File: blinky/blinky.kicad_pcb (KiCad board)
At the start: 2 copper layers, 25.4 x 25.4 mm, 7 parts, among them U1 7555

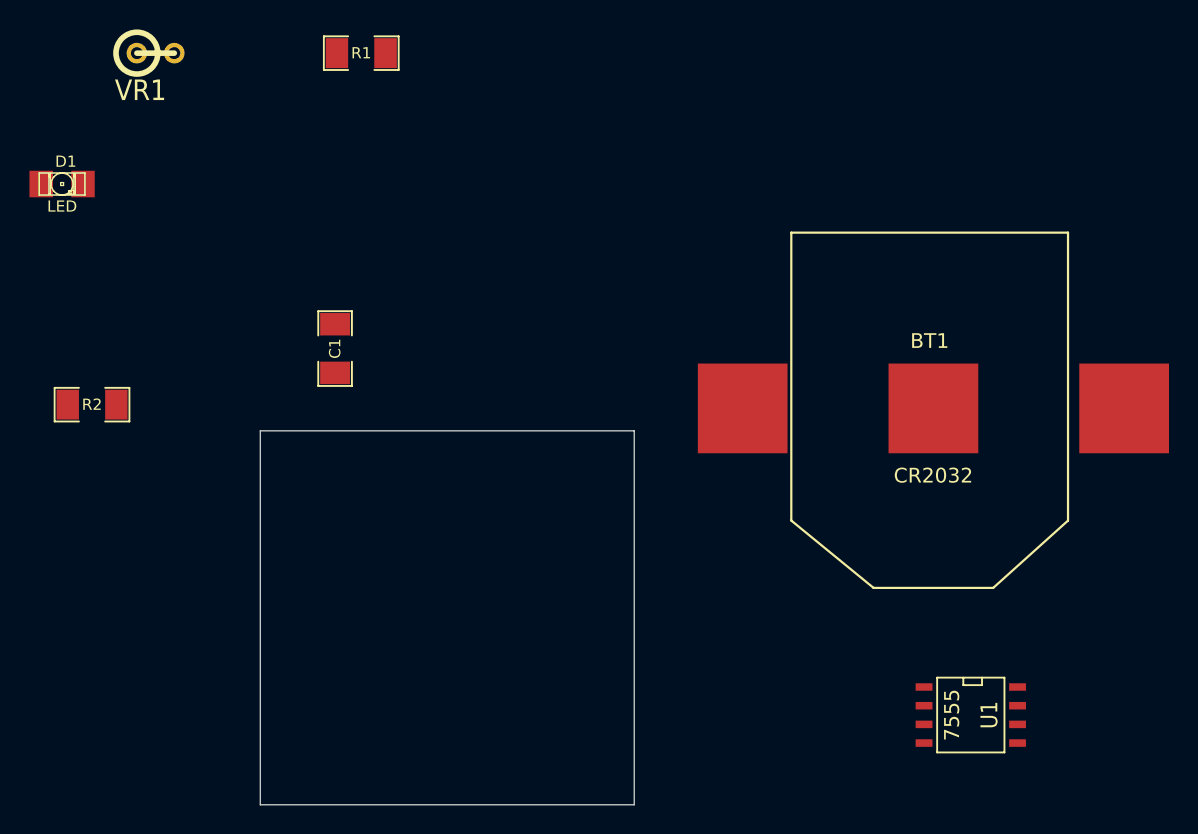
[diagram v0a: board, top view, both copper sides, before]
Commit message: Added gerbers and did layout.
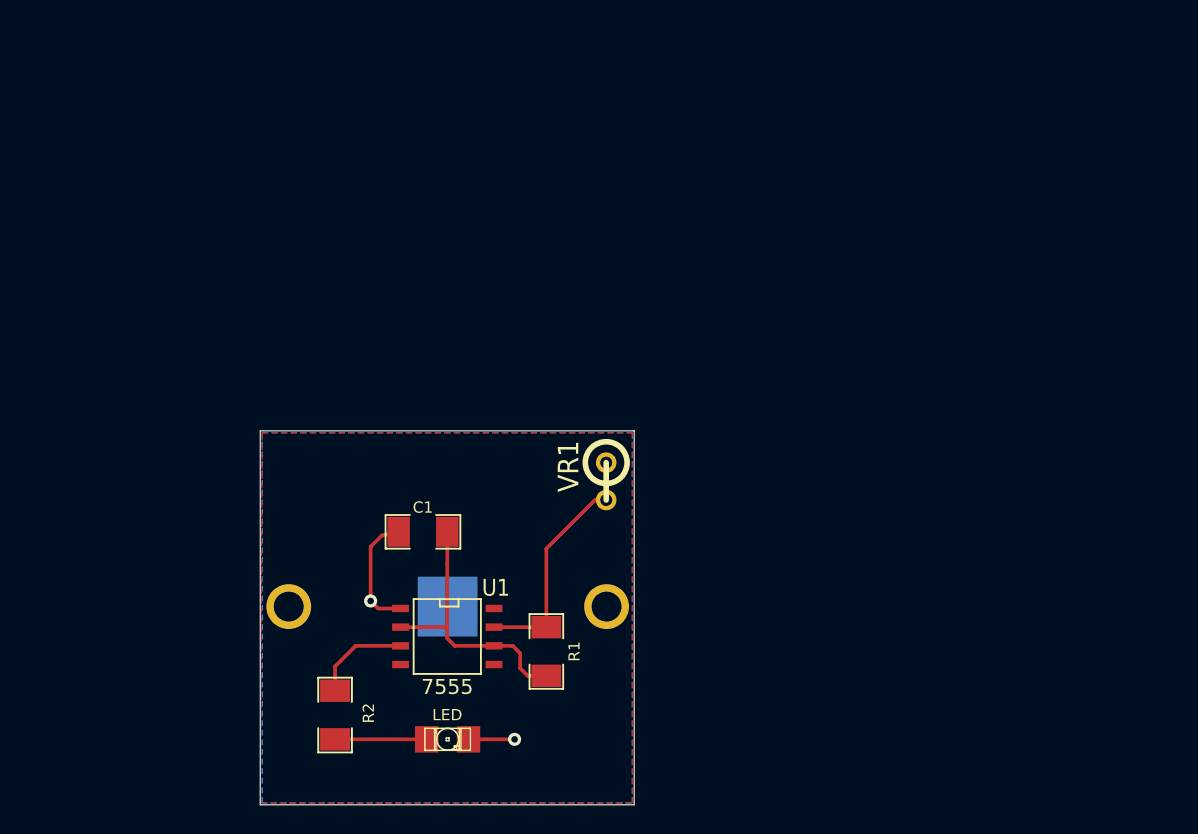
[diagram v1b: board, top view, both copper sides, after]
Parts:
- BT1: moved to B.Cu
- moved D1 45.9 mm to (40.2, 45.3)
- moved R1 42.5 mm to (46.9, 39.4), turned to 270 degrees
- moved VR1 42.2 mm to (50.9, 27.8), turned to 270 degrees
- moved U1 36.0 mm to (40.1, 38.4)
- moved BT1 35.6 mm to (40.2, 36.3), turned to 180 degrees
- moved R2 26.8 mm to (32.5, 43.7), turned to 270 degrees
- moved C1 13.8 mm to (38.5, 31.2), turned to 180 degrees
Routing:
- net N-000006: track 0.00 -> 18.8 mm
- net N-000007: track 0.00 -> 14.3 mm
- net GND: track 0.00 -> 11.3 mm, vias 0 -> 2
- net N-000001: track 0.00 -> 6.67 mm
- net N-000002: track 0.00 -> 6.23 mm
- added copper zone on B.Cu, net GND
- added copper zone on F.Cu, net VCC
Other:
- board text added: "Blinky"
